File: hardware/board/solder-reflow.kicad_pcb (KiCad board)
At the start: 2 copper layers, 128.3 x 63.5 mm, 55 parts, among them J1 AC_Con, J2 OLED 0.91, J3 PTC_Con, J4 Barrel_Jack_Switch_Pin3Ring, K1 G3MB202PDC12, Q1 BC557, SW1 RotaryEncoder_Switch, U1 TL431LP, U2 OPA2134, U3 OPA2134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

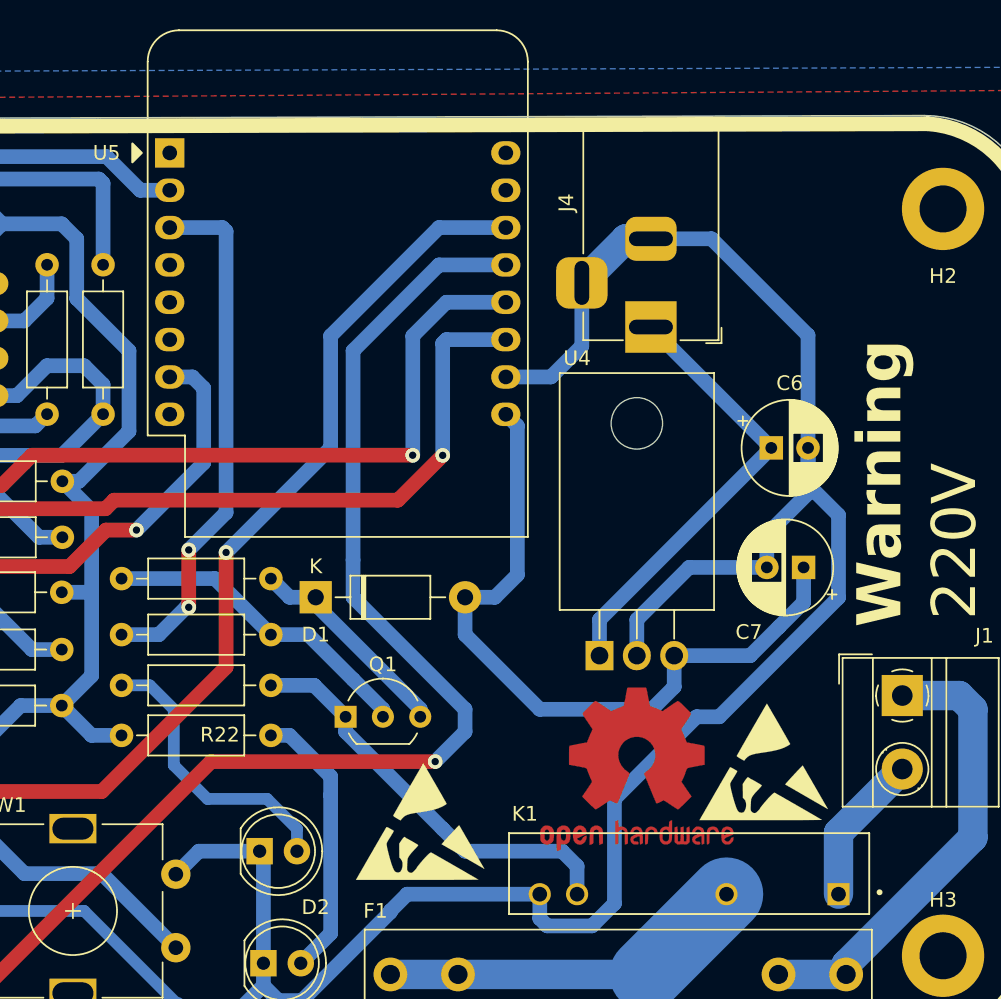
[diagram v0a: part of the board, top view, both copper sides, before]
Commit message: rotate wemos d1 mini
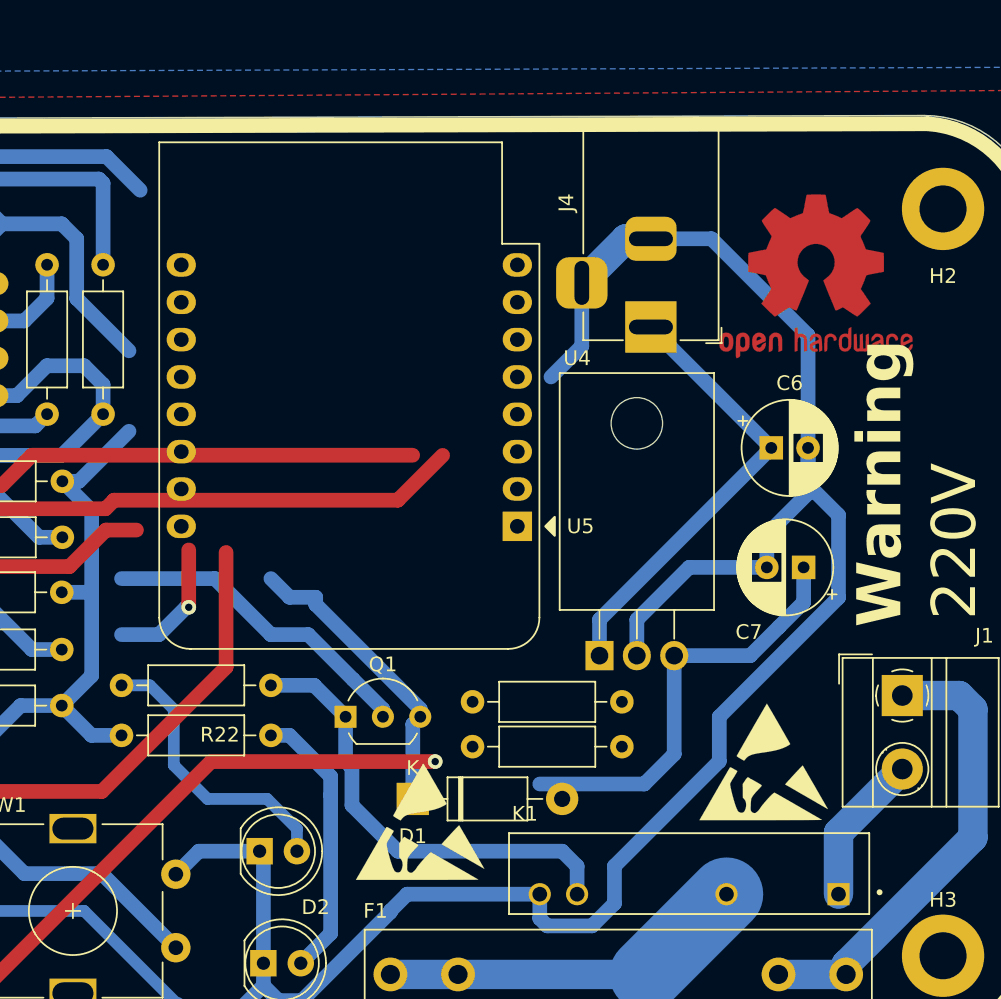
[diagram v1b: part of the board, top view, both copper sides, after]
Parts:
- moved REF** 35.7 mm to (202.2, 57.9)
- moved U5 34.7 mm to (181.9, 74.9), turned to 180 degrees
- moved R14 25.3 mm to (178.8, 86.9)
- moved R15 25.1 mm to (178.8, 89.9)
- moved D1 15.2 mm to (174.8, 93.5)
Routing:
- net /OLED_SDA: track 101.8 -> 57.1 mm
- net /OLED_SCL: track 86.1 -> 53.5 mm, vias 2 -> 1
- net /SSR_in: track 35.9 -> 9.24 mm, vias 2 -> 1
- net +5V: track 166.0 -> 140.1 mm
- net /ENC_A: track 63.9 -> 48.5 mm, vias 2 -> 1
- net /ENC_SW: track 63.6 -> 49.4 mm, vias 2 -> 1
- net /ENC_B: track 68.4 -> 56.3 mm, vias 2 -> 1
- net Net-(D1-K): track 14.6 -> 20.4 mm
- net GND: track 341.2 -> 337.3 mm
- net Net-(K1-+): track 28.8 -> 31.5 mm
- net /Sallen-Key_out: track 57.6 -> 55.6 mm

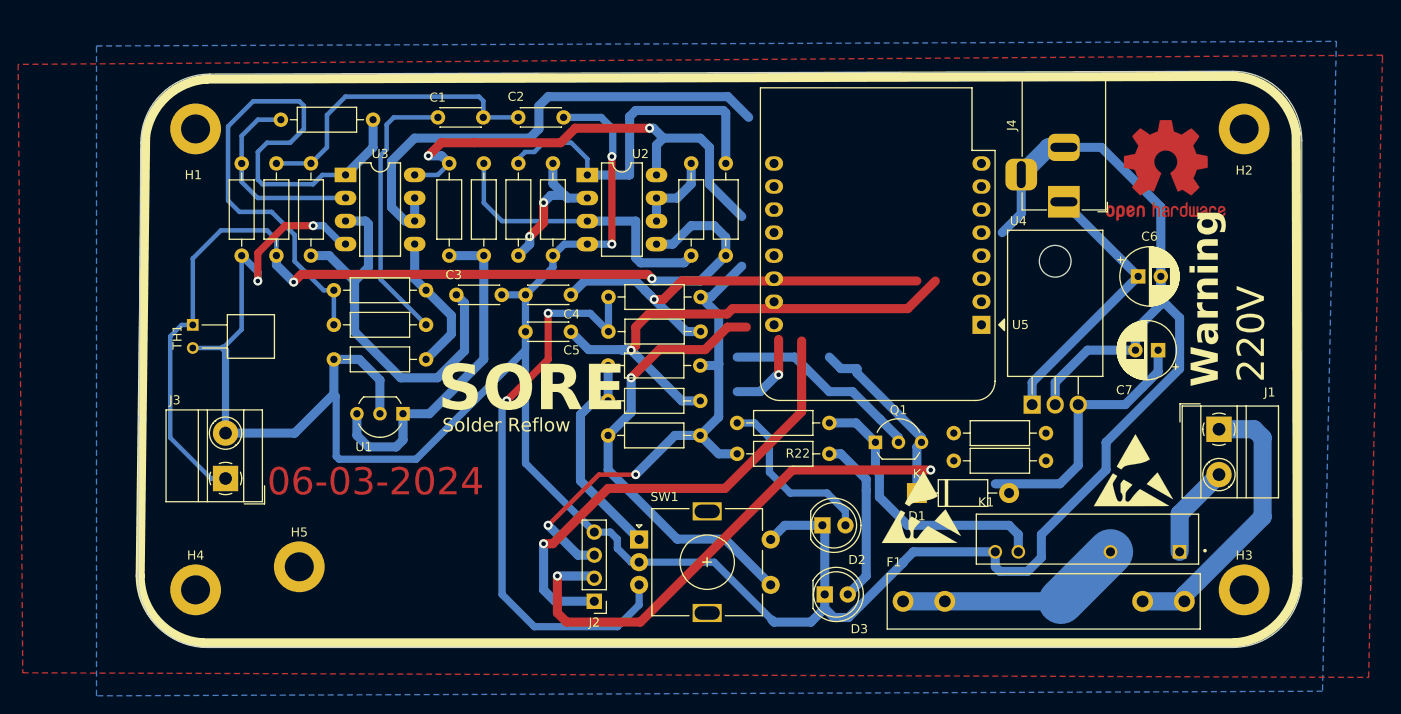
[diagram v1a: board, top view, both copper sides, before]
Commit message: route rotated wemos and make order to jlc pcb
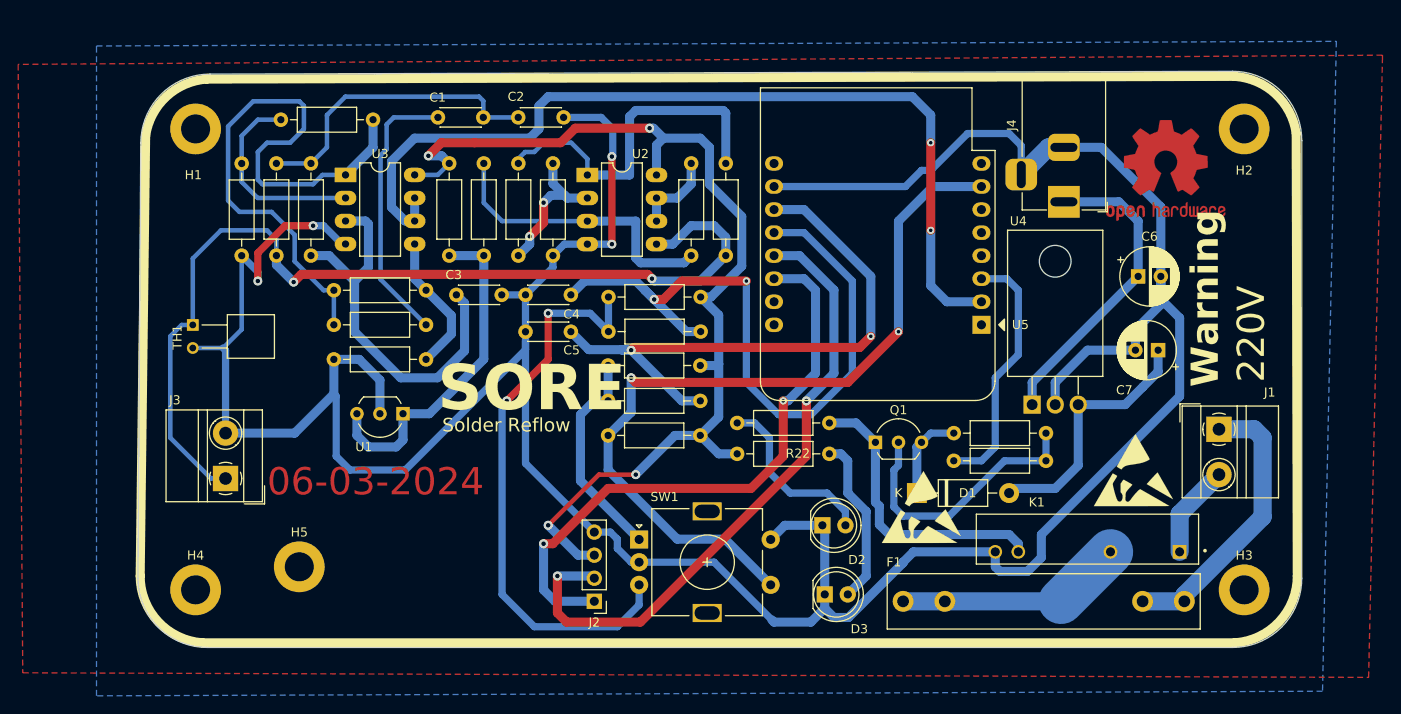
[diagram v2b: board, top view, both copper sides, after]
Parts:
- moved R14 10.2 mm to (189.0, 86.9), turned to 180 degrees
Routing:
- net /Sallen-Key_out: track 55.6 -> 100.6 mm, vias 0 -> 2
- net /ENC_SW: track 49.4 -> 89.3 mm, vias 1 -> 2
- net /ENC_A: track 48.5 -> 76.9 mm, vias 1 -> 2
- net GND: track 337.3 -> 364.4 mm
- net /SSR_in: track 9.24 -> 28.1 mm, vias 1 -> 0
- net /OLED_SDA: track 57.1 -> 71.7 mm
- net /OLED_SCL: track 53.5 -> 66.8 mm, vias 1 -> 2
- net Net-(D1-K): track 20.4 -> 9.78 mm
- net /ENC_B: track 56.3 -> 65.8 mm, vias 1 -> 2
- net Net-(Q1-B): track 22.0 -> 30.1 mm
- net +5V: track 140.1 -> 144.5 mm
- net Net-(U4-IN): track 30.6 -> 34.1 mm
- net Net-(K1-+): track 31.5 -> 32.7 mm
